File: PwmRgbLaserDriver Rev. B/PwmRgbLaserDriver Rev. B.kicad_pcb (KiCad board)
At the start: 4 copper layers, 63 x 42 mm, 54 parts, among them IC1 ADA4817-1ARDZ, IC2 ADA4817-1ARDZ, IC3 ADA4817-1ARDZ, J1 RED_IN, J2 15V, J3 RLO, J4 GREEN_IN, J5 GLO, J6 BLUE_IN, J7 BLO, Q1 Q_NPN_BCE, Q2 Q_NPN_BCE, Q3 Q_NPN_BCE, U1 TPS54331GDR

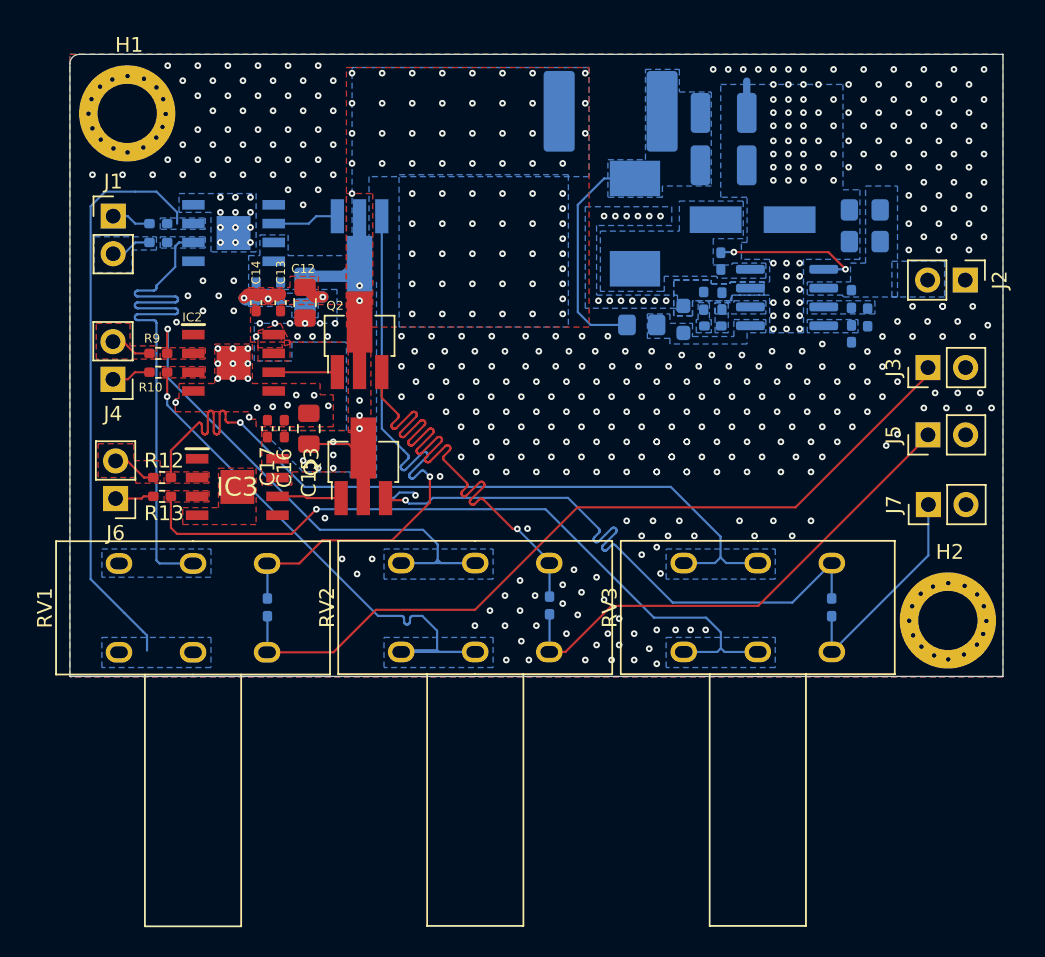
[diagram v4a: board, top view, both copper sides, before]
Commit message: Board Finished
Board has been completed. PDN finished, Silk Screen cleaned up.
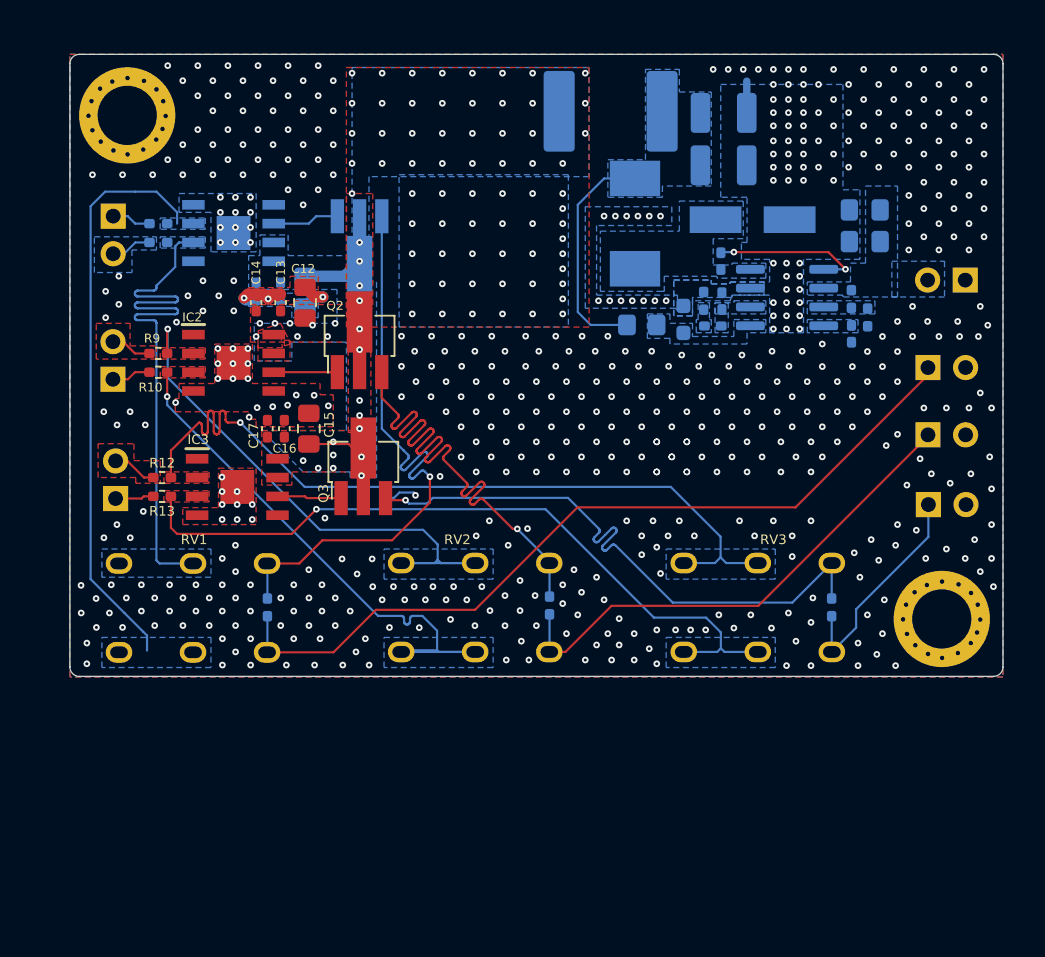
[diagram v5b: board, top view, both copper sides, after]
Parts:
- moved H2 0.42 mm to (266.0, 52.0)
- moved H1 0.14 mm to (211.0, 18.1)
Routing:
- net GND: vias 440 -> 571
- net +9V: vias 87 -> 91
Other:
- outline, holes or cut-outs redrawn
- board text added: "+"
- board text added: "-"
- board text added: "15VDC"
- board text added: "BIN"
- board text added: "BO"
- board text added: "GIN"
- board text added: "GO"
- board text added: "PwmRgbLaserDriver REV. B"
- board text added: "RIN"
- board text added: "RO"
